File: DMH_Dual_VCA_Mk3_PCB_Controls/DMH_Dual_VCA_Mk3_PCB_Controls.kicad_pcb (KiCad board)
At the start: 2 copper layers, 48 x 121 mm, 114 parts, among them J10 Conn_01x04, J11 Conn_01x04_PinHeader, J50 Conn_01x08, J60 Conn_01x08, Q5 BC548, Q6 BC548, Q7 BC548, Q8 BC548, SW1 SW_DPDT_OnOffOn_x2, SW2 SW_DPDT_3way, U3 TL074, U4 TL074, U7 TL074, U8 TL074

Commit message: KiCad 10 and updated SynthStuff
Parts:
- removed C18, C19: 2.2uF, Capacitor_THT:CP_Radial_D4.0mm_P1.50mm
- removed D13, D16: LED_R, LED_THT:LED_D3.0mm
- removed D14, D15: 1N4148, Diode_THT:D_DO-35_SOD27_P7.62mm_Horizontal
- removed R100, R92: 20k, Resistor_THT:R_Axial_DIN0207_L6.3mm_D2.5mm_P7.62mm_Horizontal
- removed R101, R93: 3k3, Resistor_THT:R_Axial_DIN0207_L6.3mm_D2.5mm_P7.62mm_Horizontal
- removed R94, R99: 100k, Resistor_THT:R_Axial_DIN0207_L6.3mm_D2.5mm_P7.62mm_Horizontal
- removed R95, R96: 1k, Resistor_THT:R_Axial_DIN0207_L6.3mm_D2.5mm_P7.62mm_Horizontal
- removed R97, R98: 330k, Resistor_THT:R_Axial_DIN0207_L6.3mm_D2.5mm_P7.62mm_Horizontal
- U4: value TL074 -> TL072; footprint Package_DIP:DIP-14_W7.62mm_Socket -> Package_DIP:DIP-8_W7.62mm_Socket
- moved J50 1.11 mm to (97.1, 83.5)
- moved J60 1.10 mm to (52.9, 122.5)
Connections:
- U4 pad 4: +12V -> -12V
- U4 pad 8: Net-(R93-Pad1) -> +12V
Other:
- board size 48 x 121 mm -> 49 x 121 mm

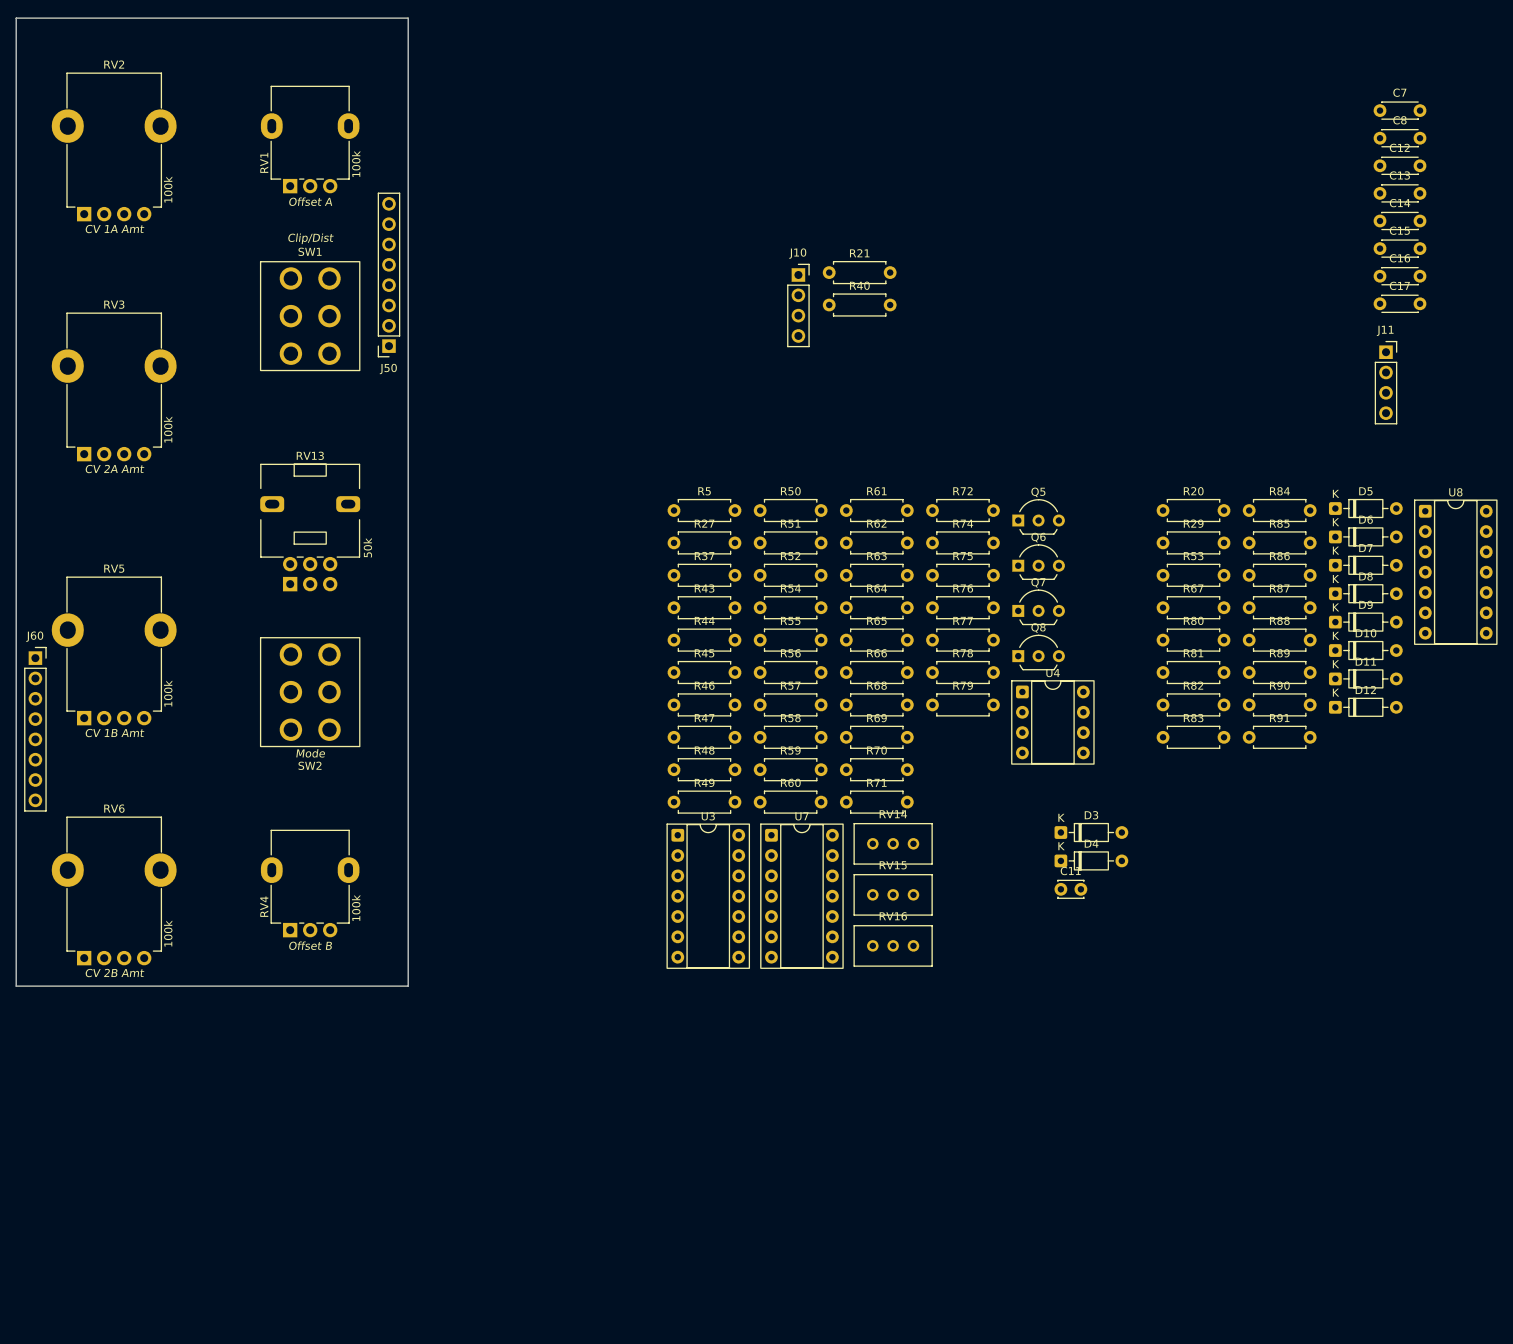
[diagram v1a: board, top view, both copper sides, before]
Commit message: Controls PCB comp placement started
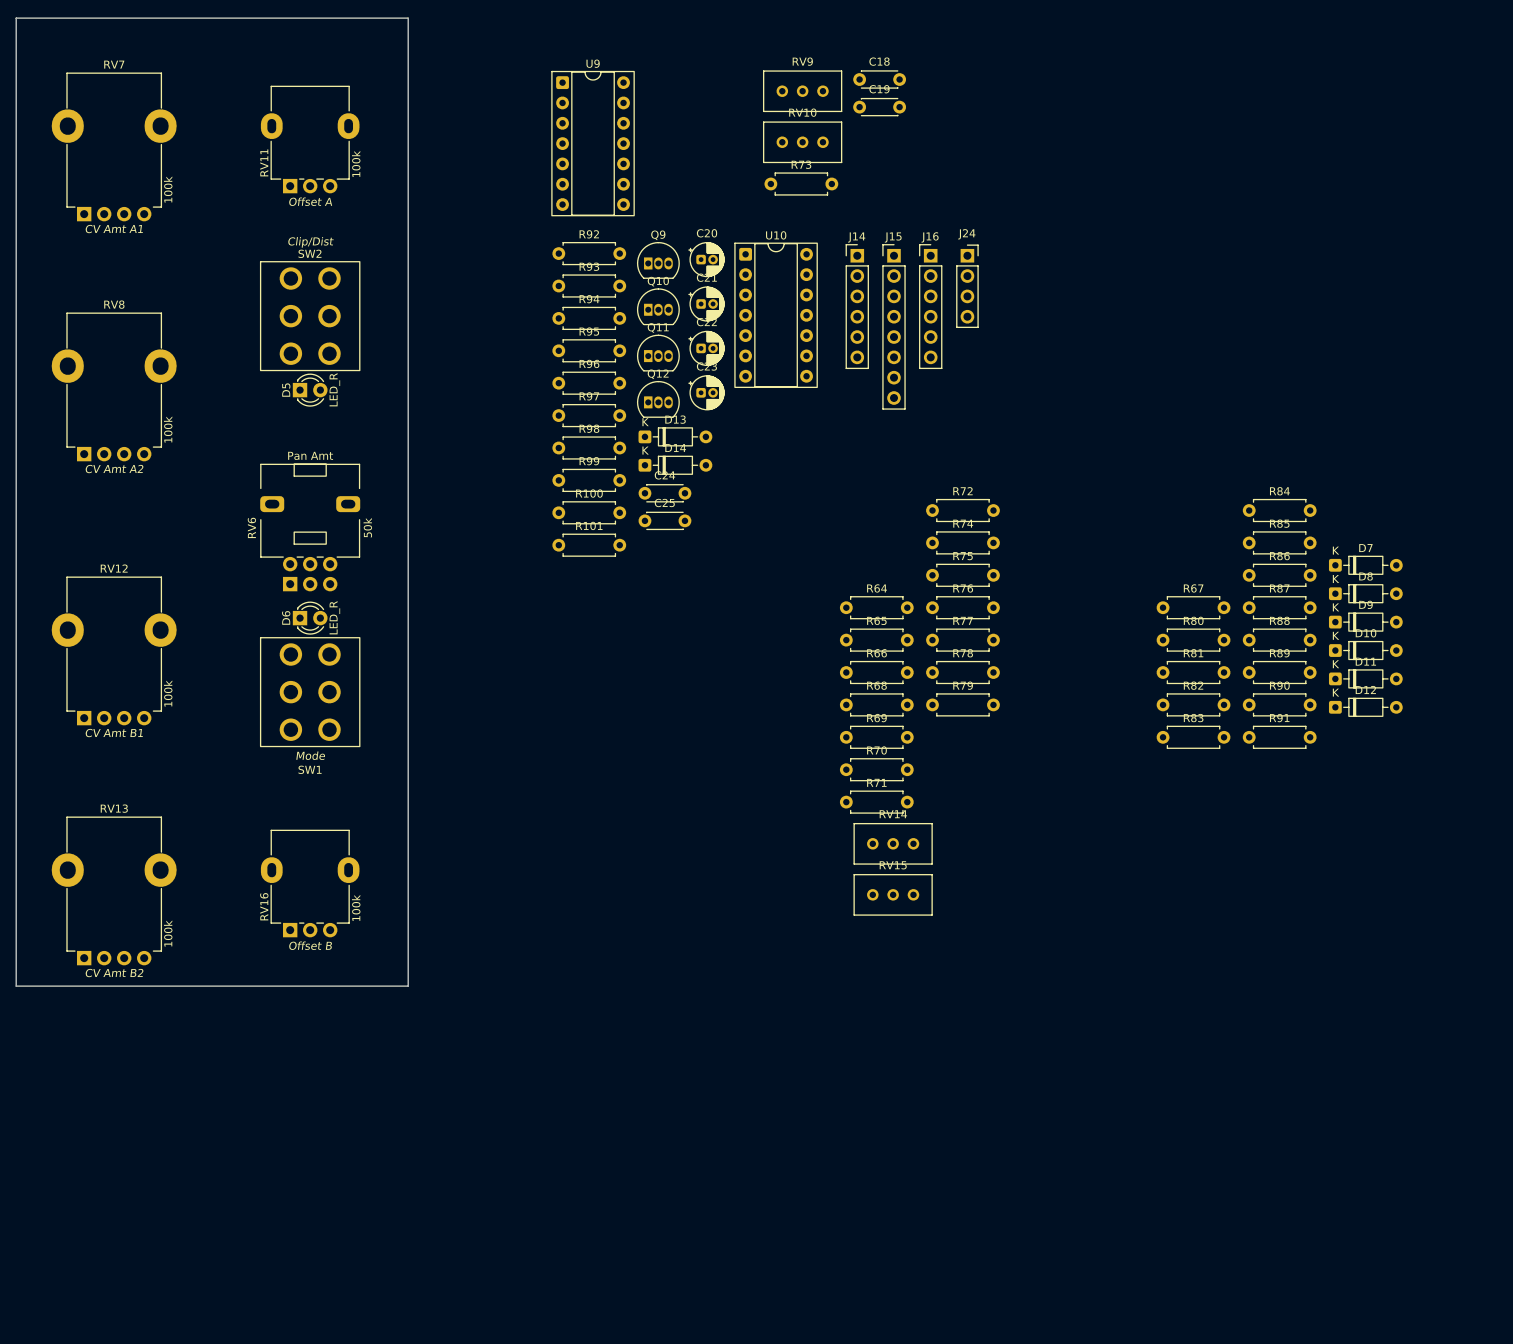
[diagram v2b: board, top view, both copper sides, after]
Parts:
- removed C11: 22pF, Capacitor_THT:C_Disc_D3.0mm_W2.0mm_P2.50mm
- removed C12, C13, C14, C15, C16, C17, C7, C8: 100nF, Capacitor_THT:C_Disc_D4.3mm_W1.9mm_P5.00mm
- removed D3, D4: 1N4148, Diode_THT:D_DO-35_SOD27_P7.62mm_Horizontal
- removed J10: Conn_01x04, Connector_PinSocket_2.54mm:PinSocket_1x04_P2.54mm_Vertical
- removed J11: Conn_01x04_PinHeader, Connector_PinSocket_2.54mm:PinSocket_1x04_P2.54mm_Vertical
- removed J50, J60: Conn_01x08, Connector_PinSocket_2.54mm:PinSocket_1x08_P2.54mm_Vertical
- removed Q5, Q6, Q7, Q8: BC548, Package_TO_SOT_THT:TO-92L_Inline_Wide
- removed R20: 2k2, Resistor_THT:R_Axial_DIN0207_L6.3mm_D2.5mm_P7.62mm_Horizontal
- removed R21, R40: 18k, Resistor_THT:R_Axial_DIN0207_L6.3mm_D2.5mm_P7.62mm_Horizontal
- removed R27, R29, R37, R5, R50, R51, R52, R53, R54, R55, R56: 100k, Resistor_THT:R_Axial_DIN0207_L6.3mm_D2.5mm_P7.62mm_Horizontal
- removed R43, R47, R57, R63: 100R, Resistor_THT:R_Axial_DIN0207_L6.3mm_D2.5mm_P7.62mm_Horizontal
- removed R44, R46, R58, R60: 20k, Resistor_THT:R_Axial_DIN0207_L6.3mm_D2.5mm_P7.62mm_Horizontal
- removed R45, R48, R49, R59, R61, R62: 10k, Resistor_THT:R_Axial_DIN0207_L6.3mm_D2.5mm_P7.62mm_Horizontal
- removed RV1, RV4: 100k, SynthStuff:Potentiometer_Alpha_RD901F-40-00D_Single_Vertical
- removed RV2, RV3, RV5: 100k, SynthStuff:Potentiometer_TT_P110KH1
- removed U3, U7, U8: TL074, Package_DIP:DIP-14_W7.62mm_Socket
- removed U4: TL072, Package_DIP:DIP-8_W7.62mm_Socket
- added C18: 100nF, Capacitor_THT:C_Disc_D4.3mm_W1.9mm_P5.00mm, F.Cu at (155.9, 50.2)
- added C19: 100nF, Capacitor_THT:C_Disc_D4.3mm_W1.9mm_P5.00mm, F.Cu at (155.9, 53.6)
- added C20: 2.2uF, Capacitor_THT:CP_Radial_D4.0mm_P1.50mm, F.Cu at (136.1, 72.7)
- added C21: 2.2uF, Capacitor_THT:CP_Radial_D4.0mm_P1.50mm, F.Cu at (136.1, 78.2)
- added C22: 22uF, Capacitor_THT:CP_Radial_D4.0mm_P1.50mm, F.Cu at (136.1, 83.8)
- added C23: 22uF, Capacitor_THT:CP_Radial_D4.0mm_P1.50mm, F.Cu at (136.1, 89.3)
- added C24: 100nF, Capacitor_THT:C_Disc_D4.3mm_W1.9mm_P5.00mm, F.Cu at (129.1, 101.9)
- added C25: 100nF, Capacitor_THT:C_Disc_D4.3mm_W1.9mm_P5.00mm, F.Cu at (129.1, 105.3)
- added D13: ZPD3V0, Diode_THT:D_DO-35_SOD27_P7.62mm_Horizontal, F.Cu at (129.1, 94.8)
- added D14: ZPD3V0, Diode_THT:D_DO-35_SOD27_P7.62mm_Horizontal, F.Cu at (129.1, 98.4)
- added J14: Conn_01x06, Connector_PinHeader_2.54mm:PinHeader_1x06_P2.54mm_Vertical, F.Cu at (155.6, 72.2)
- added J15: Conn_01x08, Connector_PinHeader_2.54mm:PinHeader_1x08_P2.54mm_Vertical, F.Cu at (160.2, 72.2)
- added J16: Conn_01x06, Connector_PinHeader_2.54mm:PinHeader_1x06_P2.54mm_Vertical, F.Cu at (164.8, 72.2)
- added J24: Conn_01x04, Connector_PinSocket_2.54mm:PinSocket_1x04_P2.54mm_Vertical, F.Cu at (169.4, 72.2)
- added Q10: BC548, Package_TO_SOT_THT:TO-92_Inline, F.Cu at (129.5, 79.0)
- added Q11: BC548, Package_TO_SOT_THT:TO-92_Inline, F.Cu at (129.5, 84.7)
- added Q12: BC548, Package_TO_SOT_THT:TO-92_Inline, F.Cu at (129.5, 90.5)
- added Q9: BC548, Package_TO_SOT_THT:TO-92_Inline, F.Cu at (129.5, 73.2)
- added R100: 1k, Resistor_THT:R_Axial_DIN0207_L6.3mm_D2.5mm_P7.62mm_Horizontal, F.Cu at (118.3, 104.3)
- added R101: 1k, Resistor_THT:R_Axial_DIN0207_L6.3mm_D2.5mm_P7.62mm_Horizontal, F.Cu at (118.3, 108.4)
- added R73: 100k, Resistor_THT:R_Axial_DIN0207_L6.3mm_D2.5mm_P7.62mm_Horizontal, F.Cu at (144.8, 63.2)
- added R92: 100k, Resistor_THT:R_Axial_DIN0207_L6.3mm_D2.5mm_P7.62mm_Horizontal, F.Cu at (118.3, 71.9)
- added R93: 100k, Resistor_THT:R_Axial_DIN0207_L6.3mm_D2.5mm_P7.62mm_Horizontal, F.Cu at (118.3, 76.0)
- added R94: 220k, Resistor_THT:R_Axial_DIN0207_L6.3mm_D2.5mm_P7.62mm_Horizontal, F.Cu at (118.3, 80.0)
- added R95: 220k, Resistor_THT:R_Axial_DIN0207_L6.3mm_D2.5mm_P7.62mm_Horizontal, F.Cu at (118.3, 84.1)
- added R96: 100k, Resistor_THT:R_Axial_DIN0207_L6.3mm_D2.5mm_P7.62mm_Horizontal, F.Cu at (118.3, 88.1)
- added R97: 100k, Resistor_THT:R_Axial_DIN0207_L6.3mm_D2.5mm_P7.62mm_Horizontal, F.Cu at (118.3, 92.2)
- added R98: 2k2, Resistor_THT:R_Axial_DIN0207_L6.3mm_D2.5mm_P7.62mm_Horizontal, F.Cu at (118.3, 96.2)
- added R99: 2k2, Resistor_THT:R_Axial_DIN0207_L6.3mm_D2.5mm_P7.62mm_Horizontal, F.Cu at (118.3, 100.3)
- added RV10: 50k, Potentiometer_THT:Potentiometer_Bourns_3296W_Vertical, F.Cu at (151.3, 58.0)
- added RV11: 100k, SynthStuff:Potentiometer_Alpha_RD901F-40-00D_Single_Vertical, F.Cu at (84.8, 63.5)
- added RV12: 100k, SynthStuff:Potentiometer_TT_P110KH1, F.Cu at (60.2, 130.0)
- added RV7: 100k, SynthStuff:Potentiometer_TT_P110KH1, F.Cu at (60.2, 67.0)
- added RV8: 100k, SynthStuff:Potentiometer_TT_P110KH1, F.Cu at (60.2, 97.0)
- added RV9: 50k, Potentiometer_THT:Potentiometer_Bourns_3296W_Vertical, F.Cu at (151.3, 51.6)
- added U10: TL074, Package_DIP:DIP-14_W7.62mm_Socket, F.Cu at (141.7, 72.0)
- added U9: TL074, Package_DIP:DIP-14_W7.62mm_Socket, F.Cu at (118.8, 50.6)
- D10, D9: value ZPD3V0 -> ZPD4V7
- D5, D6: value ZPD4V7 -> LED_R; footprint Diode_THT:D_DO-35_SOD27_P7.62mm_Horizontal -> LED_THT:LED_D3.0mm
- R64, R65, R70, R71: value 100k -> 33k
- R66, R72: value 100k -> 18k
- R68: value 33k -> 100k
- R76: value 100k -> 10k
- R77: value 20k -> 1k5
- R78: value 20k -> 10k
- R79: value 10k -> 1k5
- R82: value 220k -> 100k
- R84: value 2k2 -> 100k
- R85: value 100k -> 4k7
- R86: value 220k -> 1k
- R88: value 2k2 -> 4k7
- R89: value 2k2 -> 1k
- R90, R91: value 1k -> 2k2
- RV13: value 50k -> 100k; footprint Potentiometer_THT:Potentiometer_Alps_RK09L_Double_Vertical -> SynthStuff:Potentiometer_TT_P110KH1
- RV14, RV15: value 100k -> 50k
- RV16: value 50k -> 100k; footprint Potentiometer_THT:Potentiometer_Bourns_3296W_Vertical -> SynthStuff:Potentiometer_Alpha_RD901F-40-00D_Single_Vertical
- RV6: value 100k -> 50k; footprint SynthStuff:Potentiometer_TT_P110KH1 -> Potentiometer_THT:Potentiometer_Alps_RK09L_Double_Vertical
- SW1: value SW_DPDT_OnOffOn_x2 -> SW_DPDT_3way
- SW2: value SW_DPDT_3way -> SW_DPDT_OnOffOn_x2
- moved D5 130.3 mm to (86.0, 89.0)
- moved D6 129.8 mm to (86.0, 117.5)
- moved RV16 77.9 mm to (84.8, 156.5), turned to 90 degrees
- moved RV13 52.8 mm to (60.2, 160.0), turned to 0 degrees
- moved RV6 52.8 mm to (84.8, 113.2), turned to 90 degrees
- moved SW1 47.0 mm to (87.2, 126.8)
- moved SW2 47.0 mm to (87.2, 79.8)
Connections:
- D6 pad 1: GND -> Net-(D6-K)
- D6 pad 2: Net-(D5-A) -> Net-(D6-A)
- R64 pad 1: Net-(R64-Pad1) -> /CV_In_A1_c
- R65 pad 1: Net-(U3B-+) -> /CV_In_A2_c
- R65 pad 2: GND -> Net-(U9C--)
- R66 pad 1: /2nd VCA/Output B -> Net-(R66-Pad1)
- R66 pad 2: Net-(U3B--) -> +12V
- R67 pad 2: Net-(U8A--) -> /Processed_CV_A_c
- R68 pad 1: /2nd VCA/CV PT Input -> Net-(R68-Pad1)
- R68 pad 2: Net-(U4A--) -> /Processed_CV_A_c
- R69 pad 1: /2nd VCA/Attenuverted CV PT -> Net-(R69-Pad1)
- R69 pad 2: Net-(U4B--) -> /Processed_CV_A_c
- R70 pad 1: Net-(U4B--) -> /CV_In_B1_c
- R70 pad 2: /2nd VCA/Inverted CV PT -> Net-(U9B--)
- R71 pad 1: /2nd VCA/CV PT Offset -> /CV_In_B2_c
- R71 pad 2: Net-(U3D--) -> Net-(U9D--)
- R72 pad 1: Net-(U3D--) -> Net-(R72-Pad1)
- R72 pad 2: Net-(R45-Pad1) -> +12V
- R74 pad 1: Net-(U7B--) -> Net-(R74-Pad1)
- R74 pad 2: Net-(D3-A) -> /Processed_CV_B_c
- R75 pad 2: Net-(U7B--) -> /Processed_CV_B_c
- R76 pad 1: Net-(D4-K) -> Net-(Q9-B)
- R76 pad 2: GND -> Net-(C20-Pad2)
- R77 pad 1: Net-(U7C--) -> -12V
- R77 pad 2: Net-(R75-Pad1) -> Net-(Q9-B)
- R78 pad 1: /2nd VCA/Balanced Offset -> Net-(Q10-B)
- R78 pad 2: Net-(U7C--) -> Net-(C21-Pad2)
- R79 pad 1: -5V -> -12V
- R79 pad 2: Net-(U7C--) -> Net-(Q10-B)
- R80 pad 1: Net-(U8B--) -> /Clip_In_A_c
- R80 pad 2: Net-(R80-Pad2) -> Net-(U10A--)
- R81 pad 1: Net-(SW1A-B) -> /Clip_In_B_c
- R81 pad 2: Net-(U8B--) -> Net-(U10D--)
- R82 pad 1: Net-(D9-K) -> Net-(Q11-B)
- R82 pad 2: Net-(U8B--) -> +12V
- R83 pad 1: Net-(R83-Pad1) -> Net-(Q10-C)
- R83 pad 2: Net-(U8D--) -> +12V
- R84 pad 1: Net-(R83-Pad1) -> Net-(R84-Pad1)
- R84 pad 2: Net-(SW1B-B) -> Net-(U10A--)
- R85 pad 1: Net-(SW1B-B) -> Net-(D5-A)
- R85 pad 2: Net-(U8C--) -> +12V
- R86 pad 1: Net-(D11-K) -> -12V
- R86 pad 2: Net-(U8C--) -> Net-(D5-K)
- R87 pad 1: Net-(U8C--) -> Net-(R87-Pad1)
- R87 pad 2: Net-(R87-Pad2) -> Net-(U10D--)
- R88 pad 1: Net-(R80-Pad2) -> Net-(D6-A)
- R88 pad 2: Net-(R88-Pad2) -> +12V
- R89 pad 1: Net-(R87-Pad2) -> -12V
- R89 pad 2: Net-(R89-Pad2) -> Net-(D6-K)
- R90 pad 1: Net-(R88-Pad2) -> Net-(R84-Pad1)
- R90 pad 2: /Clipping/Output A -> Net-(SW2A-B)
- R91 pad 1: Net-(R89-Pad2) -> Net-(R87-Pad1)
- R91 pad 2: /Clipping/Output B -> Net-(SW2B-B)
- RV13 pad 2: /2nd VCA/CV PT Pot G1 -> Net-(U9D-+)
- RV13 pad 3: /2nd VCA/CV PT Input -> /CV_In_B2_c
- RV14 pad 1: -12V -> Net-(U9B--)
- RV14 pad 2: Net-(R50-Pad1) -> Net-(R74-Pad1)
- RV14 pad 3: +12V -> Net-(R74-Pad1)
- RV15 pad 1: -12V -> Net-(U9D--)
- RV15 pad 2: Net-(R64-Pad1) -> Net-(R75-Pad1)
- RV15 pad 3: +12V -> Net-(R75-Pad1)
- RV16 pad 1: Net-(U4A--) -> GND
- RV16 pad 2: /2nd VCA/Attenuverted CV PT -> Net-(R73-Pad1)
- RV16 pad 3: /2nd VCA/Attenuverted CV PT -> Net-(R72-Pad1)
- RV6 pad 2: /Inputs and Outputs/CV 2 B Pot -> /CV_PT_Pot_G1_c
- RV6 pad 3: /Inputs and Outputs/CV 2 B Jack -> /CV_In_PT_c
- SW1 pad 1: Net-(D9-K) -> +5V
- SW1 pad 2: Net-(SW1A-B) -> /CV_PT_Offset_c
- SW1 pad 3: Net-(D5-K) -> /Balanced_Offset_c
- SW1 pad 4: Net-(D11-K) -> /Inverted_CV_PT_c
- SW1 pad 5: Net-(SW1B-B) -> /Processed_CV_PT_c
- SW1 pad 6: Net-(D7-K) -> /Attenuverted_CV_PT_c
- SW2 pad 1: +5V -> Net-(D11-K)
- SW2 pad 2: /2nd VCA/CV PT Offset -> Net-(SW2A-B)
- SW2 pad 3: /2nd VCA/Balanced Offset -> Net-(D7-K)
- SW2 pad 4: /2nd VCA/Inverted CV PT -> Net-(D13-K)
- SW2 pad 5: Net-(R55-Pad1) -> Net-(SW2B-B)
- SW2 pad 6: /2nd VCA/Attenuverted CV PT -> Net-(D9-K)

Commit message: Moved clipping circuit back to main PCB
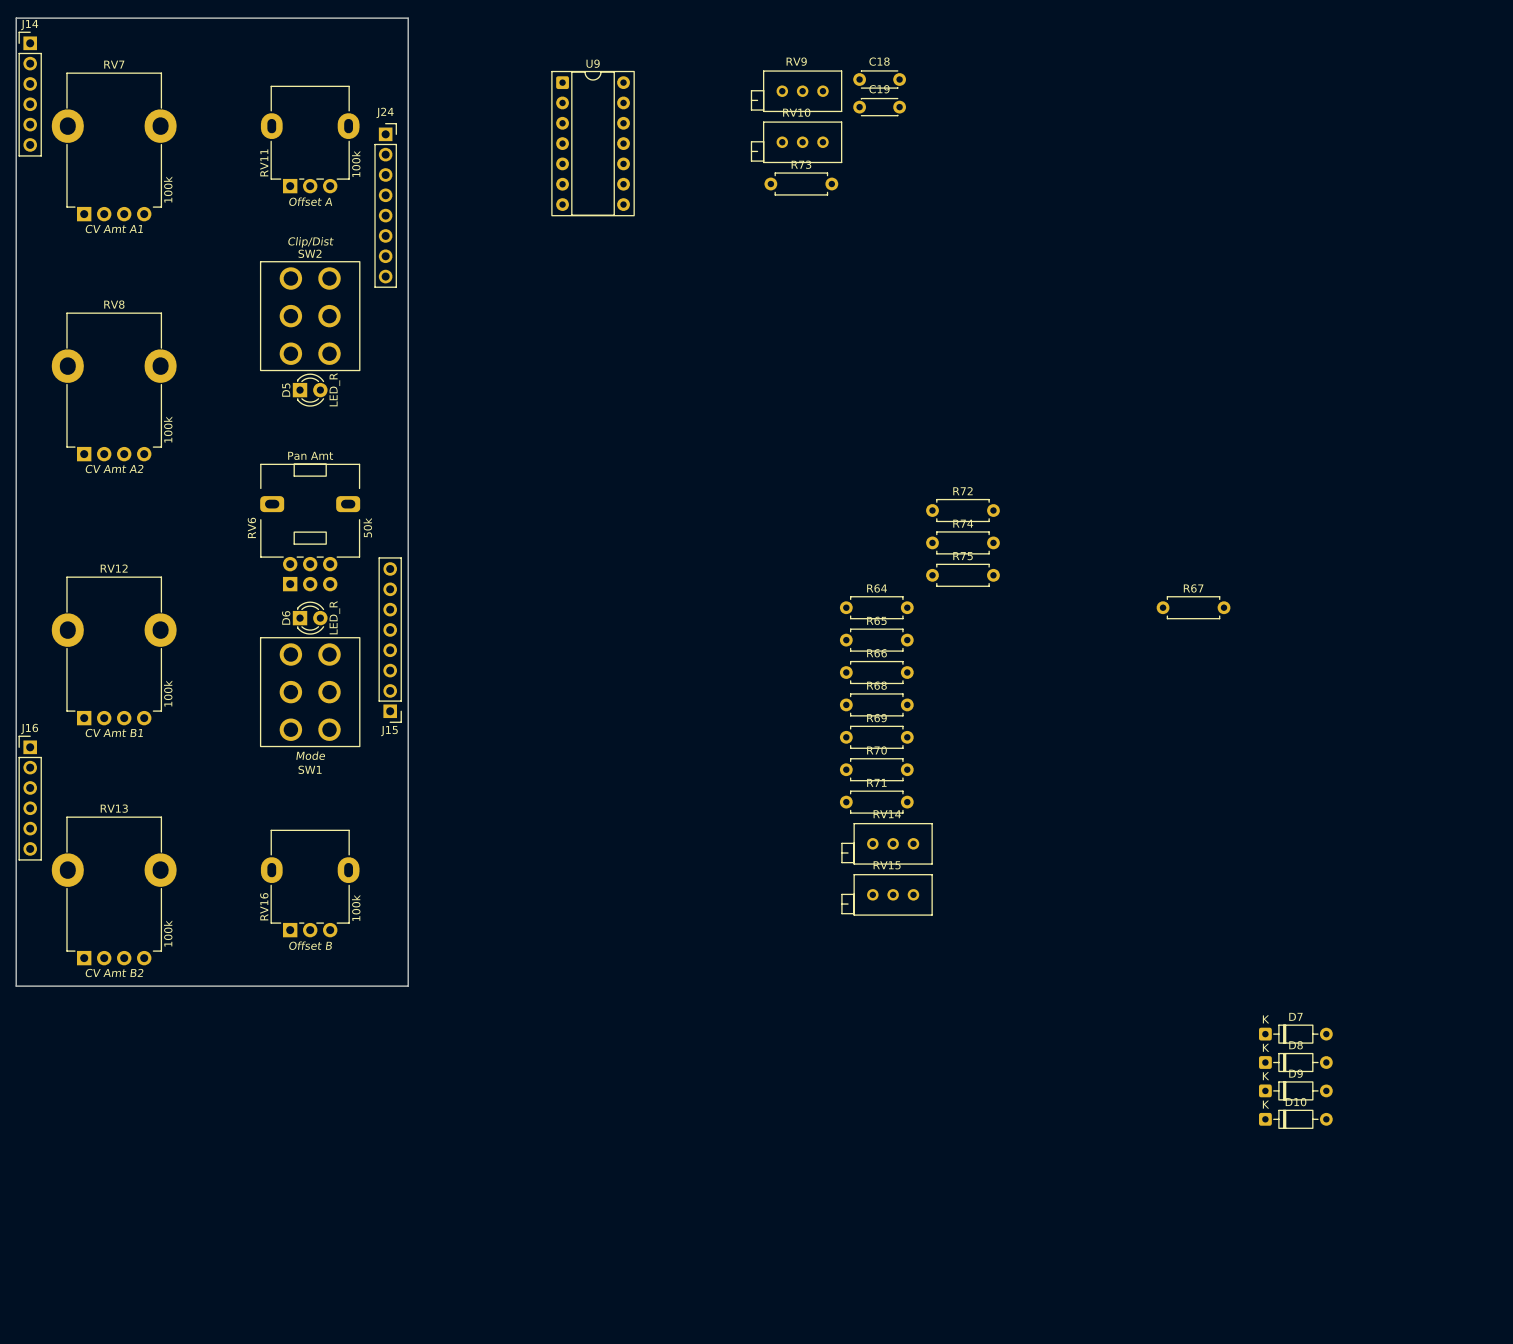
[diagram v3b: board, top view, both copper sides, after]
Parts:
- removed C20, C21: 2.2uF, Capacitor_THT:CP_Radial_D4.0mm_P1.50mm
- removed C22, C23: 22uF, Capacitor_THT:CP_Radial_D4.0mm_P1.50mm
- removed C24, C25: 100nF, Capacitor_THT:C_Disc_D4.3mm_W1.9mm_P5.00mm
- removed D11, D12, D13, D14: ZPD3V0, Diode_THT:D_DO-35_SOD27_P7.62mm_Horizontal
- removed Q10, Q11, Q12, Q9: BC548, Package_TO_SOT_THT:TO-92_Inline
- removed R100, R101, R86, R89: 1k, Resistor_THT:R_Axial_DIN0207_L6.3mm_D2.5mm_P7.62mm_Horizontal
- removed R76, R78: 10k, Resistor_THT:R_Axial_DIN0207_L6.3mm_D2.5mm_P7.62mm_Horizontal
- removed R77, R79: 1k5, Resistor_THT:R_Axial_DIN0207_L6.3mm_D2.5mm_P7.62mm_Horizontal
- removed R80, R81, R82, R83, R84, R87, R92, R93, R96, R97: 100k, Resistor_THT:R_Axial_DIN0207_L6.3mm_D2.5mm_P7.62mm_Horizontal
- removed R85, R88: 4k7, Resistor_THT:R_Axial_DIN0207_L6.3mm_D2.5mm_P7.62mm_Horizontal
- removed R90, R91, R98, R99: 2k2, Resistor_THT:R_Axial_DIN0207_L6.3mm_D2.5mm_P7.62mm_Horizontal
- removed R94, R95: 220k, Resistor_THT:R_Axial_DIN0207_L6.3mm_D2.5mm_P7.62mm_Horizontal
- removed U10: TL074, Package_DIP:DIP-14_W7.62mm_Socket
- J24: value Conn_01x04 -> Conn_01x08; footprint Connector_PinSocket_2.54mm:PinSocket_1x04_P2.54mm_Vertical -> Connector_PinSocket_2.54mm:PinSocket_1x08_P2.54mm_Vertical
- RV10, RV14, RV15, RV9: footprint Potentiometer_THT:Potentiometer_Bourns_3296W_Vertical -> Potentiometer_THT:Potentiometer_Bourns_3296X_Horizontal
- moved J16 128.2 mm to (52.2, 133.7)
- moved J14 106.7 mm to (52.2, 45.6)
- moved J15 84.9 mm to (97.2, 129.1), turned to 180 degrees
- moved J24 74.3 mm to (96.7, 57.0)
- moved D10 59.2 mm to (206.7, 180.2)
- moved D8 59.2 mm to (206.7, 173.1)
- moved D7 59.2 mm to (206.7, 169.5)
- moved D9 59.2 mm to (206.7, 176.6)
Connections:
- D5 pad 1: Net-(D5-K) -> /Clipping/LED_A_pK_c
- D5 pad 2: Net-(D5-A) -> /Clipping/LED_A_pA_c
- D6 pad 1: Net-(D6-K) -> /Clipping/LED_B_pK_c
- D6 pad 2: Net-(D6-A) -> /Clipping/LED_B_pA_c
- J24 pad 1: /Clip_In_A_c -> /Clipping/Clip_Sw_p2_c
- J24 pad 2: /Clip_In_B_c -> /Clipping/Clip_Sw_p1_c
- J24 pad 3: /Clip_Out_A_c -> /Clipping/Clip_Sw_p5_c
- J24 pad 4: /Clip_Out_B_c -> /Clipping/Clip_Sw_p4_c
- SW2 pad 1: Net-(D11-K) -> /Clipping/Clip_Sw_p1_c
- SW2 pad 2: Net-(SW2A-B) -> /Clipping/Clip_Sw_p2_c
- SW2 pad 4: Net-(D13-K) -> /Clipping/Clip_Sw_p4_c
- SW2 pad 5: Net-(SW2B-B) -> /Clipping/Clip_Sw_p5_c
